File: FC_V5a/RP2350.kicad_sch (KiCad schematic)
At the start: 29 parts, among them SW4 SW_Push, U11 W25Q128JVS, U18 RP2350_60QFN, Y1 ABM8-272-T3

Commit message: Initial V5a Layout Complete
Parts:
- removed R95: 1k, Resistor_SMD:R_0402_1005Metric, symbol Device:R
- removed SW4: SW_Push, Button_Switch_SMD:SW_Push_1P1T_NO_Vertical_Wuerth_434133025816, symbol Switch:SW_Push
- U11: footprint Package_SO:SOIC-8_5.23x5.23mm_P1.27mm -> Package_SO:SOIC-8_5.3x5.3mm_P1.27mm
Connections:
- net GPIO0 is gone; now on net TX: R9.1
- net RTC_INT: now also U18.41 (GPIO27_ADC1); no longer U18.40 (GPIO26_ADC0)
- net SPI0_CS1: no longer U18.41 (GPIO27_ADC1)
- net ~{MUX_RESET}: now also U18.40 (GPIO26_ADC0); no longer U18.33 (GPIO21)
- net QSPI_SS renamed BOOTSEL

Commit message: Initial DRC Errors Cleaned Up
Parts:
- R2: value DNF -> 10k
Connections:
- net RF2_IO0: now also U18.35 (GPIO23)
- net RF2_RX_EN: now also U18.33 (GPIO21)
- net RF2_TX_EN: now also U18.34 (GPIO22)
- net ~{GPIO_EXPANDER_RESET}: now reaches U18.32 (GPIO20)
- net USB_D+ renamed USB_DP
- net USB_D- renamed USB_DM
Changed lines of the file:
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@@
+		)
+	)
+	(global_label "~{GPIO_EXPANDER_RESET}"
+		(shape output)
+		(at 209.55 123.19 0)
+		(fields_autoplaced yes)
+		(effects
+			(font
+				(size 1.27 1.27)
+			)
+			(justify left)
+		)
+		(property "Intersheetrefs" "${INTERSHEET_REFS}"
+			(at 234.4274 123.19 0)
+			(effects
+				(font
+					(size 1.27 1.27)
+				)
+				(justify left)
+				(hide yes)
+			)
+		)
+	)
+	(global_label "RF2_TX_EN"
+		(shape input)
+		(at 209.55 128.27 0)
+		(fields_autoplaced yes)
+		(effects
+			(font
+				(size 1.27 1.27)
+			)
+			(justify left)
+		)
+		(property "Intersheetrefs" "${INTERSHEET_REFS}"
+			(at 222.6951 128.27 0)
+			(effects
+				(font
+					(size 1.27 1.27)
+				)
+				(justify left)
+				(hide yes)
+			)
 		)
 	)
@@
 		(property "Intersheetrefs" "${INTERSHEET_REFS}"
 			(at 221.327 107.95 0)
+			(effects
+				(font
+					(size 1.27 1.27)
+				)
+				(justify left)
+				(hide yes)
+			)
+		)
+	)
+	(global_label "RF2_IO0"
+		(shape bidirectional)
+		(at 209.55 130.81 0)
+		(fields_autoplaced yes)
+		(effects
+			(font
+				(size 1.27 1.27)
+			)
+			(justify left)
+		)
+		(property "Intersheetrefs" "${INTERSHEET_REFS}"
+			(at 221.327 130.81 0)
 			(effects
 				(font
@@
 		)
 	)
-	(global_label "RF2_IO0"
-		(shape bidirectional)
-		(at 234.95 115.57 0)
-		(fields_autoplaced yes)
-		(effects
-			(font
-				(size 1.27 1.27)
-			)
-			(justify left)
-		)
-		(property "Intersheetrefs" "${INTERSHEET_REFS}"
-			(at 246.727 115.57 0)
-			(effects
-				(font
-					(size 1.27 1.27)
-				)
-				(justify left)
-				(hide yes)
-			)
-		)
-	)
 	(global_label "~{FIRE_DEPLOY1_A}"
 		(shape output)
@@
 		)
 	)
-	(global_label "USB_D-"
+	(global_label "USB_DM"
 		(shape input)
 		(at 224.79 64.77 0)
@@
 		)
 		(property "Intersheetrefs" "${INTERSHEET_REFS}"
-			(at 235.3952 64.77 0)
+			(at 235.2742 64.77 0)
 			(effects
 				(font
@@
 		)
 	)
-	(global_label "RF2_TX_EN"
-		(shape input)
-		(at 234.95 113.03 0)
-		(fields_autoplaced yes)
-		(effects
-			(font
-				(size 1.27 1.27)
-			)
-			(justify left)
-		)
-		(property "Intersheetrefs" "${INTERSHEET_REFS}"
-			(at 248.0951 113.03 0)
-			(effects
-				(font
-					(size 1.27 1.27)
-				)
-				(justify left)
-				(hide yes)
-			)
-		)
-	)
 	(global_label "SWDIO"
 		(shape input)
@@
 		)
 	)
-	(global_label "SPI0_CS1"
-		(shape output)
-		(at 247.65 129.54 0)
-		(fields_autoplaced yes)
-		(effects
-			(font
-				(size 1.27 1.27)
-			)
-			(justify left)
-		)
-		(property "Intersheetrefs" "${INTERSHEET_REFS}"
-			(at 259.5856 129.54 0)
-			(effects
-				(font
-					(size 1.27 1.27)
-				)
-				(justify left)
-				(hide yes)
-			)
-		)
-	)
 	(global_label "FC_RESET"
 		(shape bidirectional)
@@
 		(property "Intersheetrefs" "${INTERSHEET_REFS}"
 			(at 224.3002 85.0106 0)
+			(effects
+				(font
+					(size 1.27 1.27)
+				)
+				(justify left)
+				(hide yes)
+			)
+		)
+	)
+	(global_label "RF1_IO4"
+		(shape bidirectional)
+		(at 209.55 102.87 0)
+		(fields_autoplaced yes)
+		(effects
+			(font
+				(size 1.27 1.27)
+			)
+			(justify left)
+		)
+		(property "Intersheetrefs" "${INTERSHEET_REFS}"
+			(at 139.7 -39.37 0)
+			(effects
+				(font
+					(size 1.27 1.27)
+				)
+				(hide yes)
+			)
+		)
+	)
+	(global_label "SPI1_SCK"
+		(shape output)
+		(at 209.55 118.11 0)
+		(fields_autoplaced yes)
+		(effects
+			(font
+				(size 1.27 1.27)
+			)
+			(justify left)
+		)
+		(property "Intersheetrefs" "${INTERSHEET_REFS}"
+			(at 221.5461 118.11 0)
+			(effects
+				(font
+					(size 1.27 1.27)
+				)
+				(justify left)
+				(hide yes)
+			)
+		)
+	)
+	(global_label "WDT_ENABLE"
+		(shape output)
+		(at 209.55 135.89 0)
+		(fields_autoplaced yes)
+		(effects
+			(font
+				(size 1.27 1.27)
+			)
+			(justify left)
+		)
+		(property "Intersheetrefs" "${INTERSHEET_REFS}"
+			(at 224.207 135.89 0)
+			(effects
+				(font
+					(size 1.27 1.27)
+				)
+				(justify left)
+				(hide yes)
+			)
+		)
+	)
+	(global_label "TX"
+		(shape bidirectional)
+		(at 217.17 72.39 0)
+		(fields_autoplaced yes)
+		(effects
+			(font
+				(size 1.27 1.27)
+			)
+			(justify left)
+		)
+		(property "Intersheetrefs" "${INTERSHEET_REFS}"
+			(at 223.3642 72.39 0)
 			(effects
 				(font
@@
 	(global_label "RF2_RX_EN"
 		(shape input)
-		(at 234.95 110.49 0)
-		(fields_autoplaced yes)
-		(effects
-			(font
-				(size 1.27 1.27)
-			)
-			(justify left)
-		)
-		(property "Intersheetrefs" "${INTERSHEET_REFS}"
-			(at 248.3975 110.49 0)
-			(effects
-				(font
-					(size 1.27 1.27)
-				)
-				(justify left)
-				(hide yes)
-			)
-		)
-	)
-	(global_label "RF1_IO4"
-		(shape bidirectional)
-		(at 209.55 102.87 0)
-		(fields_autoplaced yes)
-		(effects
-			(font
-				(size 1.27 1.27)
-			)
-			(justify left)
-		)
-		(property "Intersheetrefs" "${INTERSHEET_REFS}"
-			(at 139.7 -39.37 0)
-			(effects
-				(font
-					(size 1.27 1.27)
-				)
-				(hide yes)
-			)
-		)
-	)
-	(global_label "SPI1_SCK"
-		(shape output)
-		(at 209.55 118.11 0)
-		(fields_autoplaced yes)
-		(effects
-			(font
-				(size 1.27 1.27)
-			)
-			(justify left)
-		)
-		(property "Intersheetrefs" "${INTERSHEET_REFS}"
-			(at 221.5461 118.11 0)
-			(effects
-				(font
-					(size 1.27 1.27)
-				)
-				(justify left)
-				(hide yes)
-			)
-		)
-	)
-	(global_label "WDT_ENABLE"
-		(shape output)
-		(at 209.55 135.89 0)
-		(fields_autoplaced yes)
-		(effects
-			(font
-				(size 1.27 1.27)
-			)
-			(justify left)
-		)
-		(property "Intersheetrefs" "${INTERSHEET_REFS}"
-			(at 224.207 135.89 0)
-			(effects
-				(font
-					(size 1.27 1.27)
-				)
-				(justify left)
-				(hide yes)
-			)
-		)
-	)
-	(global_label "TX"
-		(shape bidirectional)
-		(at 217.17 72.39 0)
-		(fields_autoplaced yes)
-		(effects
-			(font
-				(size 1.27 1.27)
-			)
-			(justify left)
-		)
-		(property "Intersheetrefs" "${INTERSHEET_REFS}"
-			(at 223.3642 72.39 0)
+		(at 209.55 125.73 0)
+		(fields_autoplaced yes)
+		(effects
+			(font
+				(size 1.27 1.27)
+			)
+			(justify left)
+		)
+		(property "Intersheetrefs" "${INTERSHEET_REFS}"
+			(at 222.9975 125.73 0)
 			(effects
 				(font
@@
 		)
 	)
-	(global_label "USB_D+"
+	(global_label "USB_DP"
 		(shape input)
 		(at 224.79 62.23 0)
@@
 		)
 		(property "Intersheetrefs" "${INTERSHEET_REFS}"
-			(at 235.3952 62.23 0)
+			(at 235.0928 62.23 0)
 			(effects
 				(font
@@
 			)
 		)
-		(property "Value" "DNF"
+		(property "Value" "10k"
 			(at 51.308 92.583 0)
 			(effects

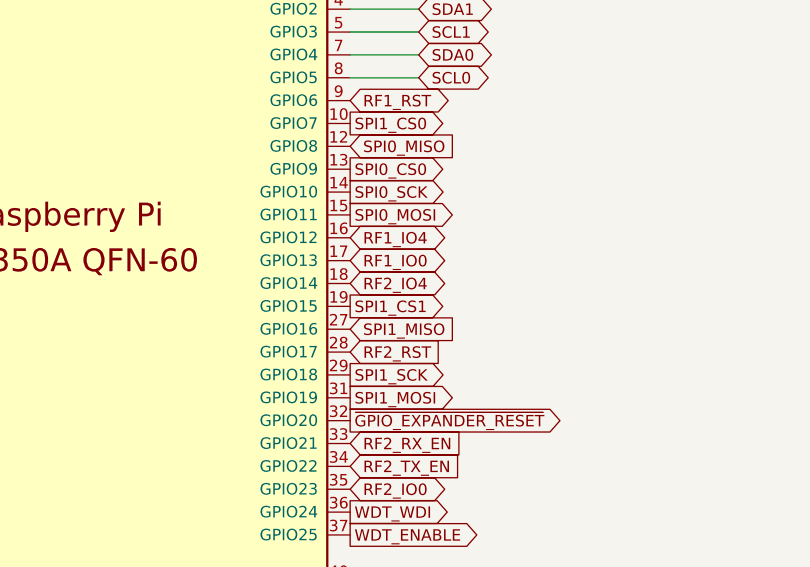
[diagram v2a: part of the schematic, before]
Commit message: Swaped RF2 to E28-2G4M27S
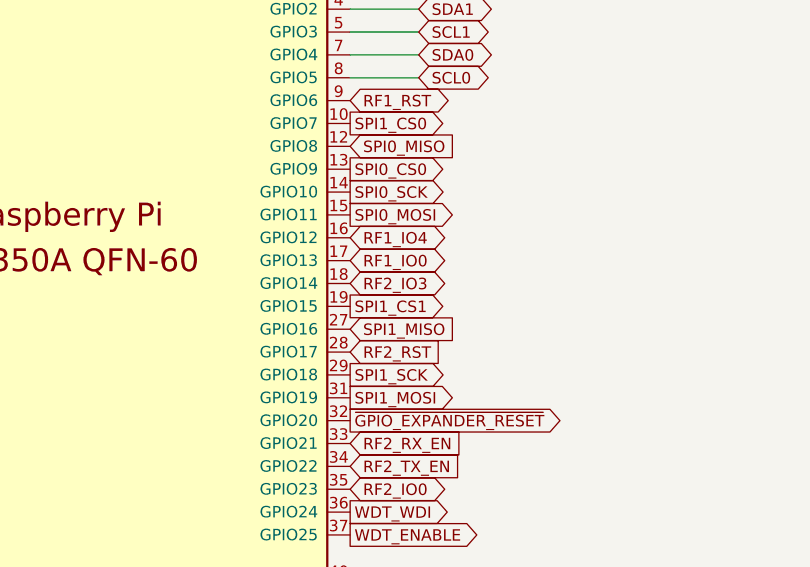
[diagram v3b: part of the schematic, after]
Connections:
- net RF2_IO4 renamed RF2_IO3
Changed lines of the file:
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@@
 		)
 	)
-	(global_label "RF2_IO4"
+	(global_label "RF2_IO3"
 		(shape bidirectional)
 		(at 209.55 107.95 0)
